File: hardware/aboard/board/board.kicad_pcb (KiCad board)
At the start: 2 copper layers, 68.6 x 53.3 mm, 41 parts, among them J1 Conn_01x04_Male, P1 Power, P2 Analog, P3 Digital, P4 Digital, P5 CONN_01X01, P6 CONN_01X01, P7 CONN_01X01, P8 CONN_01X01, U1 24LC512, U10 ST25DV04K, U2 AT25SF081-SSHD-X, U3 24LC512, U4 AT25SF081-SSHD-X, U5 24LC512, U6 LTC3406ES5, U8 Si5351A, U9 ICE40UP5K-SG48ITR, Y1 Crystal

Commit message: board for OM13088UL: process 4
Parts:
- Y1: value Crystal -> Crystal_GND24; footprint Crystal:Crystal_SMD_5032-2Pin_5.0x3.2mm -> Crystal:Crystal_SMD_5032-4Pin_5.0x3.2mm
- moved U8 29.7 mm to (153.2, 83.7)
- moved Y1 22.0 mm to (147.1, 83.7), turned to 90 degrees
- moved C3 18.3 mm to (152.1, 81.2), turned to 180 degrees
- moved C4 17.8 mm to (156.3, 81.2)
- moved U5 9.19 mm to (147.1, 90.8)
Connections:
- Y1 pad 1: Net-(U8-Pad2) -> Net-(U8-Pad3)
- Y1 pad 2: Net-(U8-Pad3) -> GND
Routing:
- net +3V3: track 0.00 -> 109.4 mm
- net SCL: track 32.0 -> 13.9 mm
- net SDA: track 31.4 -> 18.1 mm
- net Net-(U8-Pad2): track 0.00 -> 7.12 mm
- net Net-(U8-Pad3): track 0.00 -> 3.67 mm
- net GND: track 0.00 -> 1.08 mm, vias 0 -> 14

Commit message: board for OM13088UL: process 5
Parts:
- moved C5 48.3 mm to (114.6, 83.4), turned to 90 degrees
- moved C7 45.2 mm to (113.9, 89.5), turned to 90 degrees
- moved C15 42.4 mm to (119.4, 122.7), turned to 90 degrees
- moved C14 38.6 mm to (115.8, 111.4), turned to 90 degrees
- moved C16 37.1 mm to (122.7, 116.7)
- moved C12 36.7 mm to (118.3, 104.1), turned to 270 degrees
- moved C2 34.4 mm to (133.3, 118.2), turned to 90 degrees
- moved C6 31.7 mm to (129.0, 87.9)
- moved C13 31.2 mm to (128.8, 113.2), turned to 90 degrees
- moved R2 27.8 mm to (138.0, 115.8), turned to 180 degrees
- moved U6 27.8 mm to (138.8, 118.7)
- moved L1 26.9 mm to (134.6, 122.6)
- moved R3 22.7 mm to (167.3, 102.4)
- moved U2 21.2 mm to (164.8, 108.4)
- moved U4 21.2 mm to (161.9, 113.9)
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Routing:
- net +3V3: track 109.4 -> 203.9 mm, vias 0 -> 7
- net CSFPGA: track 0.00 -> 78.2 mm, vias 0 -> 5
- net CDONE: track 0.00 -> 66.8 mm, vias 0 -> 3
- net CRESET: track 0.00 -> 62.5 mm, vias 0 -> 3
- net 1V8: track 0.00 -> 62.4 mm, vias 0 -> 2
- net MISO: track 0.00 -> 53.8 mm, vias 0 -> 3
- net SCK: track 0.00 -> 53.3 mm, vias 0 -> 3
- net MOSI: track 0.00 -> 52.0 mm, vias 0 -> 3
- net Net-(R1-Pad2): track 0.00 -> 5.71 mm
- net Net-(L1-Pad2): track 0.00 -> 3.51 mm
- net GND: track 1.08 -> 3.83 mm, vias 14 -> 94

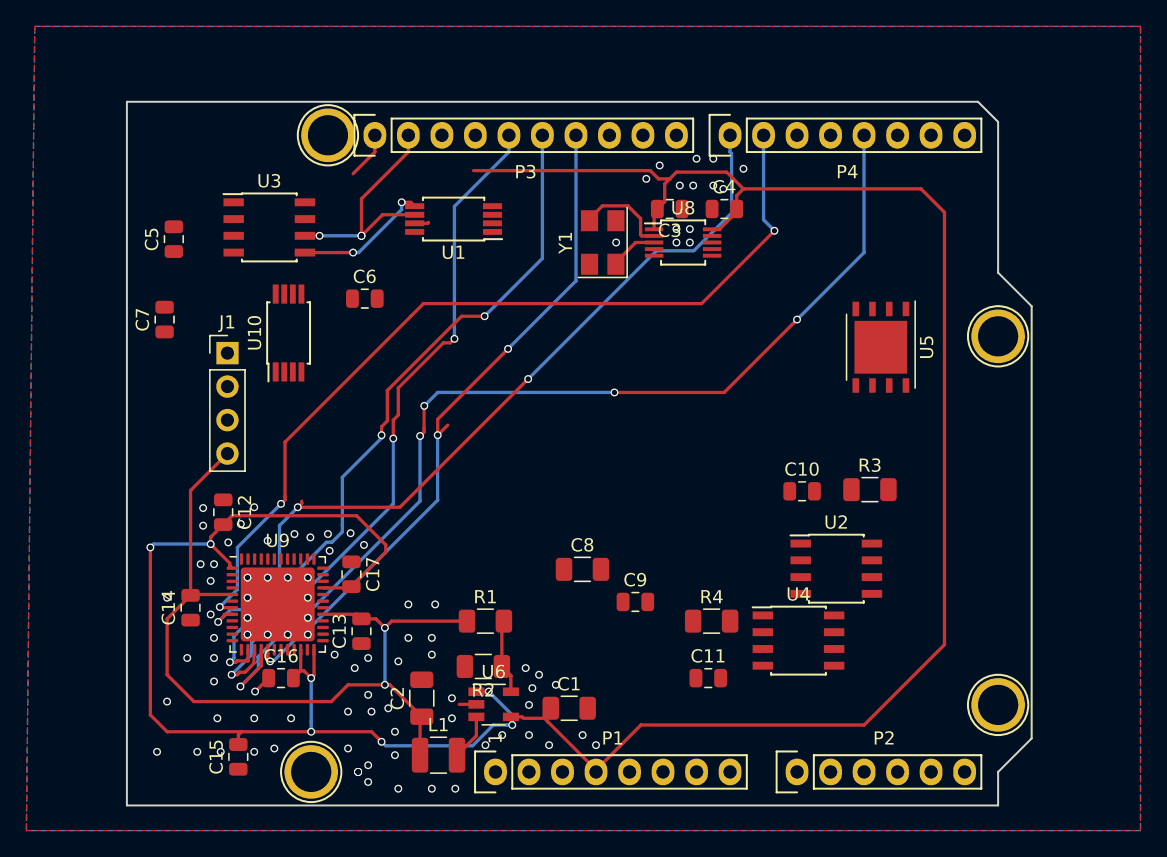
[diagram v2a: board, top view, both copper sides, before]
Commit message: board for OM13088UL: process 6
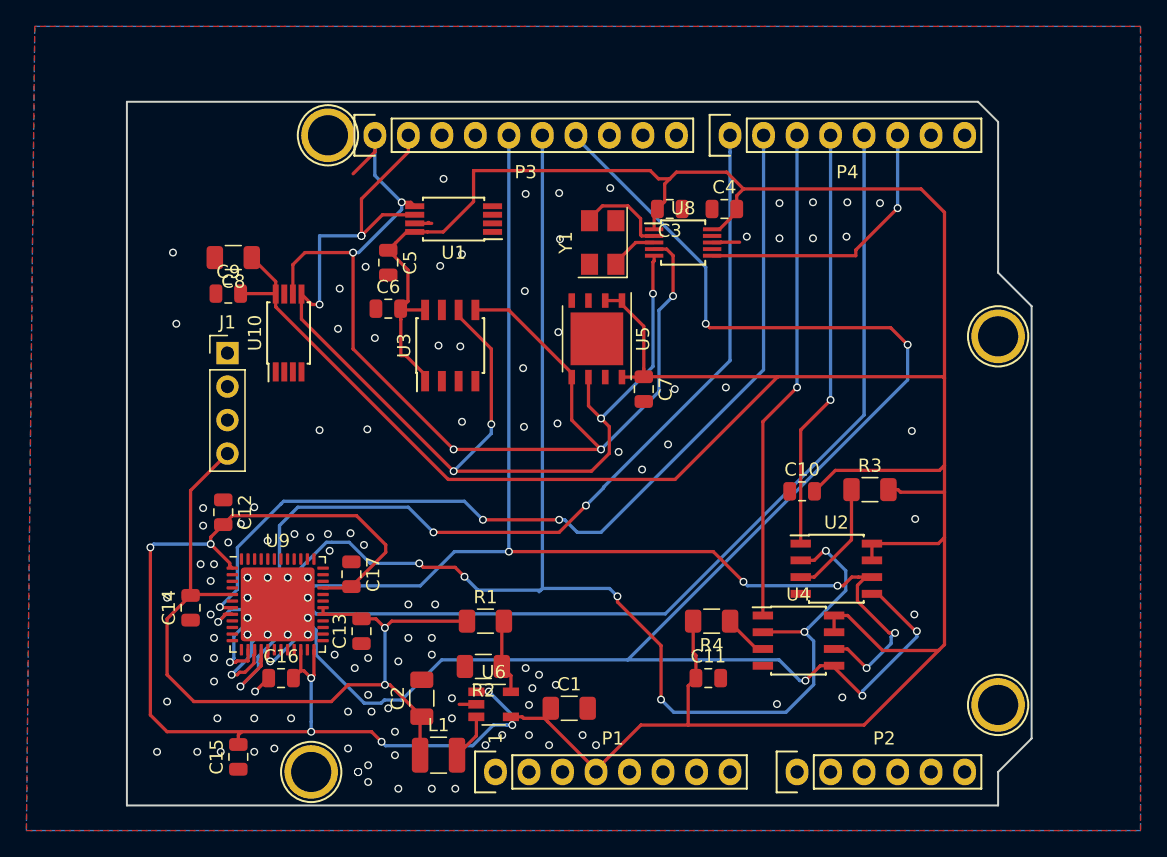
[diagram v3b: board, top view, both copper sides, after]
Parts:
- moved C9 38.7 mm to (118.7, 87.6)
- moved C7 36.7 mm to (150.2, 94.8), turned to 270 degrees
- moved C8 35.5 mm to (119.1, 84.8), turned to 180 degrees
- moved U5 21.5 mm to (146.6, 91.0)
- moved U3 16.4 mm to (135.5, 91.5), turned to 90 degrees
- moved C5 16.4 mm to (130.8, 85.2), turned to 270 degrees
- moved C6 1.93 mm to (130.8, 88.7)
- turned R4 to 180 degrees
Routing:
- net +3V3: track 203.9 -> 354.5 mm
- net MOSI: track 52.0 -> 132.3 mm, vias 3 -> 6
- net SCL: track 13.9 -> 87.2 mm, vias 2 -> 5
- net SDA: track 18.1 -> 89.3 mm, vias 3 -> 7
- net MISO: track 53.8 -> 113.0 mm, vias 3 -> 7
- net SCK: track 53.3 -> 102.2 mm, vias 3 -> 6
- net CSFLASH1: track 0.00 -> 37.5 mm, vias 0 -> 1
- net CSFLASH0: track 0.00 -> 31.9 mm, vias 0 -> 1
- net COUNTER: track 0.00 -> 22.6 mm, vias 0 -> 1
- net Net-(R3-Pad1): track 0.00 -> 8.82 mm
- net CRESET: track 62.5 -> 70.0 mm
- net CDONE: track 66.8 -> 71.2 mm
- net CSFPGA: track 78.2 -> 81.9 mm, vias 5 -> 1
- net Net-(R4-Pad1): track 0.00 -> 3.42 mm
- net GND: track 3.83 -> 6.23 mm, vias 94 -> 121
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
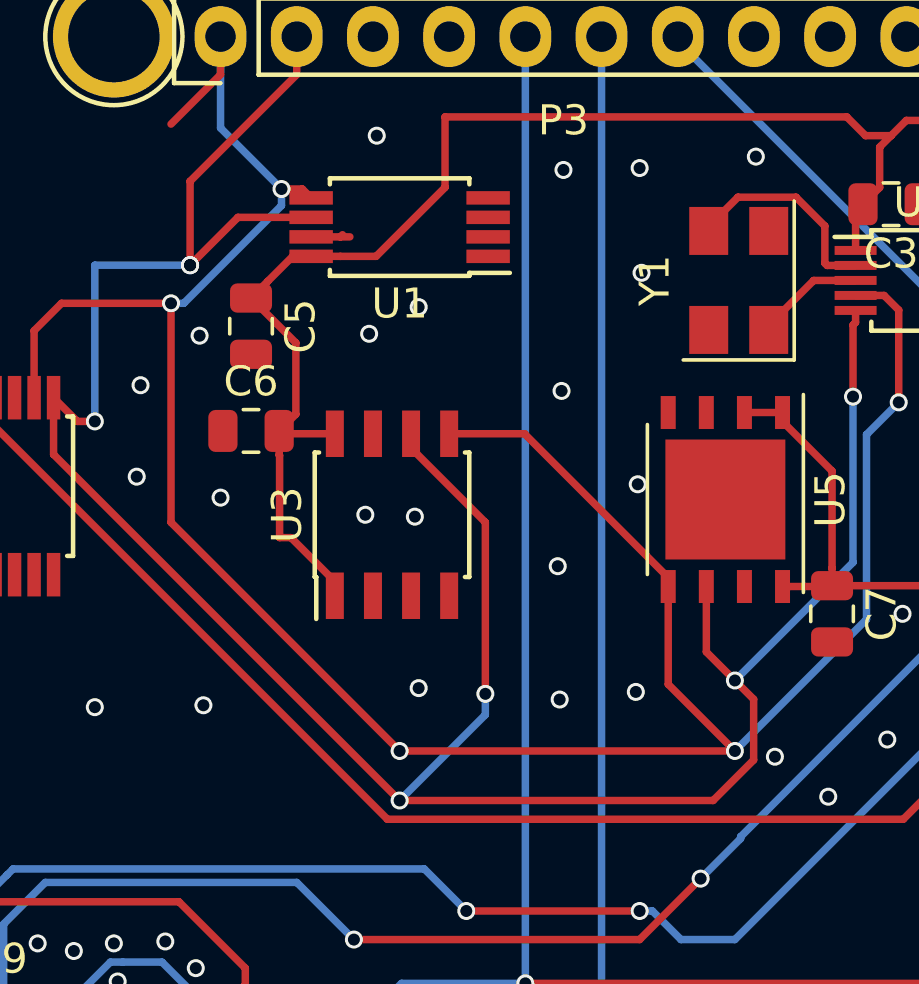
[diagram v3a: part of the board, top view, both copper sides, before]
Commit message: board for OM13088UL: fixed SCL/SDA issue
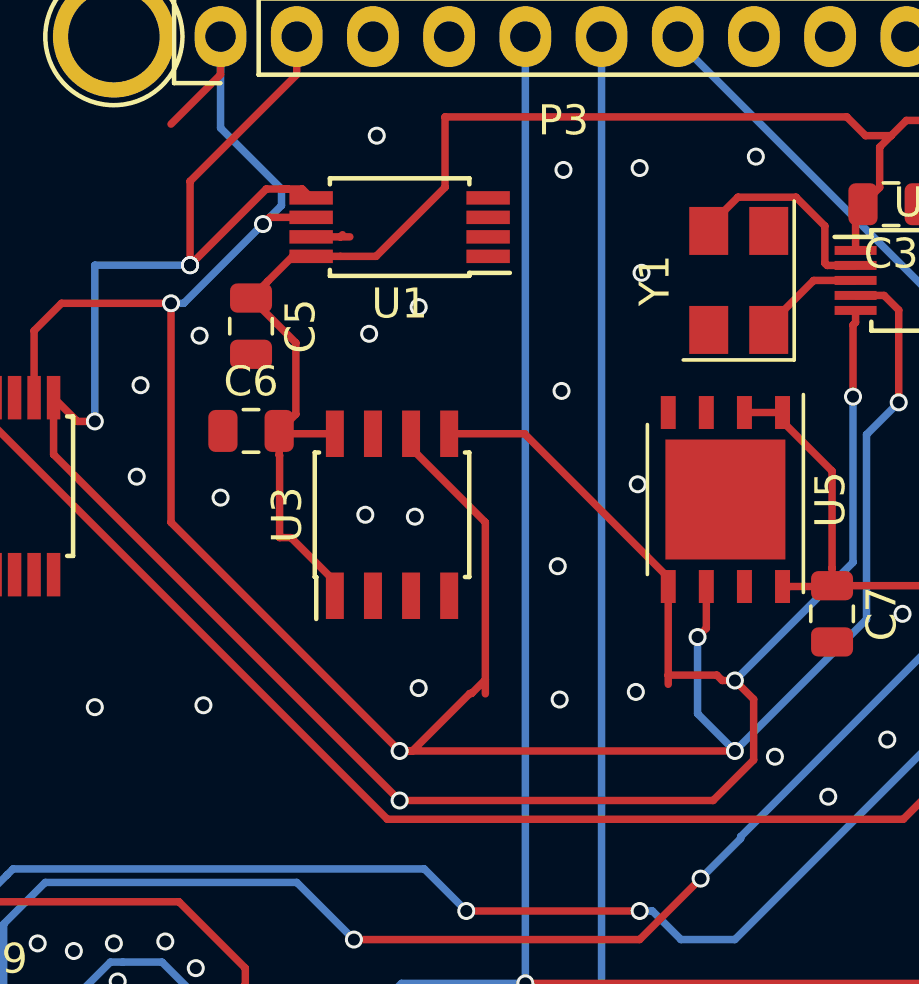
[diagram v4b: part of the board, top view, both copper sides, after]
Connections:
- U1 pad 5: SCL -> SDA
- U1 pad 6: SDA -> SCL
- U3 pad 5: SCL -> SDA
- U3 pad 6: SDA -> SCL
- U5 pad 5: SCL -> SDA
- U5 pad 6: SDA -> SCL
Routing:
- net SCL: track 87.2 -> 91.5 mm, vias 5 -> 6
- net SDA: track 89.3 -> 87.2 mm, vias 7 -> 6
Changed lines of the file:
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@@
     (thickness 1.6)
     (drawings 27)
-    (tracks 588)
+    (tracks 600)
     (zones 0)
     (modules 41)
@@
       (net 4 GND))
     (pad 5 smd rect (at 2.95 0.975 180) (size 1.45 0.45) (layers F.Cu F.Paste F.Mask)
+      (net 29 SDA))
+    (pad 6 smd rect (at 2.95 0.325 180) (size 1.45 0.45) (layers F.Cu F.Paste F.Mask)
       (net 28 SCL))
-    (pad 6 smd rect (at 2.95 0.325 180) (size 1.45 0.45) (layers F.Cu F.Paste F.Mask)
-      (net 29 SDA))
     (pad 7 smd rect (at 2.95 -0.325 180) (size 1.45 0.45) (layers F.Cu F.Paste F.Mask)
       (net 4 GND))
@@
       (net 4 GND))
     (pad 5 smd rect (at 2.7 1.905 90) (size 1.55 0.6) (layers F.Cu F.Paste F.Mask)
+      (net 29 SDA))
+    (pad 6 smd rect (at 2.7 0.635 90) (size 1.55 0.6) (layers F.Cu F.Paste F.Mask)
       (net 28 SCL))
-    (pad 6 smd rect (at 2.7 0.635 90) (size 1.55 0.6) (layers F.Cu F.Paste F.Mask)
-      (net 29 SDA))
     (pad 7 smd rect (at 2.7 -0.635 90) (size 1.55 0.6) (layers F.Cu F.Paste F.Mask)
       (net 4 GND))
@@
       (net 4 GND))
     (pad 5 smd rect (at 2.9 1.905 180) (size 0.5 1.1) (layers F.Cu F.Paste F.Mask)
+      (net 29 SDA))
+    (pad 6 smd rect (at 2.9 0.635 180) (size 0.5 1.1) (layers F.Cu F.Paste F.Mask)
       (net 28 SCL))
-    (pad 6 smd rect (at 2.9 0.635 180) (size 0.5 1.1) (layers F.Cu F.Paste F.Mask)
-      (net 29 SDA))
     (pad 7 smd rect (at 2.9 -0.635 180) (size 0.5 1.1) (layers F.Cu F.Paste F.Mask)
       (net 4 GND))
@@
   (via (at 128.143 84.455) (size 0.6) (drill 0.4) (layers F.Cu B.Cu) (net 28))
   (segment (start 131.826 81.196264) (end 131.826 80.645) (width 0.25) (layer B.Cu) (net 28))
-  (via (at 131.826 80.645) (size 0.6) (drill 0.4) (layers F.Cu B.Cu) (net 28))
   (segment (start 128.143 84.455) (end 128.567264 84.455) (width 0.25) (layer B.Cu) (net 28))
-  (segment (start 128.567264 84.455) (end 131.826 81.196264) (width 0.25) (layer B.Cu) (net 28))
-  (segment (start 132.518 80.645) (end 132.813 80.94) (width 0.25) (layer F.Cu) (net 28))
-  (segment (start 131.826 80.645) (end 132.518 80.645) (width 0.25) (layer F.Cu) (net 28))
+  (segment (start 128.567264 84.455) (end 131.208864 81.8134) (width 0.25) (layer B.Cu) (net 28))
+  (segment (start 132.518 80.645) (end 132.813 80.94) (width 0.25) (layer F.Cu) (net 29))
   (segment (start 151.912 84.193) (end 152.4 84.681) (width 0.25) (layer F.Cu) (net 28))
   (segment (start 150.962 84.193) (end 151.912 84.193) (width 0.25) (layer F.Cu) (net 28))
@@
   (via (at 146.939 99.3775) (size 0.6) (drill 0.4) (layers F.Cu B.Cu) (net 28))
   (segment (start 151.32601 94.99049) (end 146.939 99.3775) (width 0.25) (layer B.Cu) (net 28))
-  (segment (start 144.7165 97.155) (end 144.7165 93.8955) (width 0.25) (layer F.Cu) (net 28))
-  (segment (start 146.939 99.3775) (end 144.7165 97.155) (width 0.25) (layer F.Cu) (net 28))
   (segment (start 146.939 99.3775) (end 135.763 99.3775) (width 0.25) (layer F.Cu) (net 28))
   (via (at 135.763 99.3775) (size 0.6) (drill 0.4) (layers F.Cu B.Cu) (net 28))
-  (segment (start 144.7165 93.5955) (end 144.7165 93.8955) (width 0.25) (layer F.Cu) (net 28))
-  (segment (start 139.9245 88.8035) (end 144.7165 93.5955) (width 0.25) (layer F.Cu) (net 28))
-  (segment (start 137.414 88.8035) (end 139.9245 88.8035) (width 0.25) (layer F.Cu) (net 28))
+  (segment (start 144.7165 93.5955) (end 144.7165 93.8955) (width 0.25) (layer F.Cu) (net 29))
+  (segment (start 139.9245 88.8035) (end 144.7165 93.5955) (width 0.25) (layer F.Cu) (net 29))
+  (segment (start 137.414 88.8035) (end 139.9245 88.8035) (width 0.25) (layer F.Cu) (net 29))
   (segment (start 128.143 91.7575) (end 128.143 84.455) (width 0.25) (layer F.Cu) (net 28))
   (segment (start 135.763 99.3775) (end 128.143 91.7575) (width 0.25) (layer F.Cu) (net 28))
@@
   (via (at 128.778 83.185) (size 0.6) (drill 0.4) (layers F.Cu B.Cu) (net 29))
   (segment (start 128.778 83.185) (end 125.603 83.185) (width 0.25) (layer B.Cu) (net 29))
-  (segment (start 130.373 81.59) (end 132.813 81.59) (width 0.25) (layer F.Cu) (net 29))
-  (segment (start 128.778 83.185) (end 130.373 81.59) (width 0.25) (layer F.Cu) (net 29))
   (segment (start 150.962 85.093) (end 150.876 85.179) (width 0.25) (layer F.Cu) (net 29))
   (segment (start 150.962 84.693) (end 150.962 85.093) (width 0.25) (layer F.Cu) (net 29))
@@
   (via (at 146.939 97.028) (size 0.6) (drill 0.4) (layers F.Cu B.Cu) (net 29))
   (segment (start 150.876 93.091) (end 146.939 97.028) (width 0.25) (layer B.Cu) (net 29))
-  (segment (start 145.9865 96.0755) (end 145.9865 93.8955) (width 0.25) (layer F.Cu) (net 29))
-  (segment (start 146.939 97.028) (end 145.9865 96.0755) (width 0.25) (layer F.Cu) (net 29))
   (segment (start 147.564001 99.677501) (end 146.213002 101.0285) (width 0.25) (layer F.Cu) (net 29))
   (segment (start 146.213002 101.0285) (end 135.763 101.0285) (width 0.25) (layer F.Cu) (net 29))
@@
   (via (at 135.763 101.0285) (size 0.6) (drill 0.4) (layers F.Cu B.Cu) (net 29))
   (segment (start 147.564001 97.653001) (end 147.564001 99.677501) (width 0.25) (layer F.Cu) (net 29))
-  (segment (start 136.144 89.2785) (end 138.6205 91.755) (width 0.25) (layer F.Cu) (net 29))
-  (segment (start 136.144 88.8035) (end 136.144 89.2785) (width 0.25) (layer F.Cu) (net 29))
-  (via (at 138.6205 97.4725) (size 0.6) (drill 0.4) (layers F.Cu B.Cu) (net 29))
-  (segment (start 138.6205 91.755) (end 138.6205 97.4725) (width 0.25) (layer F.Cu) (net 29))
-  (segment (start 138.6205 98.171) (end 135.763 101.0285) (width 0.25) (layer B.Cu) (net 29))
-  (segment (start 138.6205 97.4725) (end 138.6205 98.171) (width 0.25) (layer B.Cu) (net 29))
+  (segment (start 136.144 89.2785) (end 138.6205 91.755) (width 0.25) (layer F.Cu) (net 28))
+  (segment (start 136.144 88.8035) (end 136.144 89.2785) (width 0.25) (layer F.Cu) (net 28))
+  (segment (start 136.187264 99.3775) (end 138.104964 97.4598) (width 0.25) (layer F.Cu) (net 28))
+  (segment (start 135.763 99.3775) (end 136.187264 99.3775) (width 0.25) (layer F.Cu) (net 28))
+  (segment (start 138.1633 97.4598) (end 138.6205 97.0026) (width 0.25) (layer F.Cu) (net 28))
+  (segment (start 138.104964 97.4598) (end 138.1633 97.4598) (width 0.25) (layer F.Cu) (net 28))
+  (segment (start 138.6205 91.755) (end 138.6205 97.0026) (width 0.25) (layer F.Cu) (net 28))
+  (segment (start 138.6205 97.0026) (end 138.6205 97.4725) (width 0.25) (layer F.Cu) (net 28))
+  (via (at 145.6944 95.5802) (size 0.6) (drill 0.4) (layers F.Cu B.Cu) (net 28))
+  (segment (start 145.9865 93.8955) (end 145.9865 95.2881) (width 0.25) (layer F.Cu) (net 28))
+  (segment (start 145.9865 95.2881) (end 145.6944 95.5802) (width 0.25) (layer F.Cu) (net 28))
+  (segment (start 145.6944 98.1329) (end 146.939 99.3775) (width 0.25) (layer B.Cu) (net 28))
+  (segment (start 145.6944 95.5802) (end 145.6944 98.1329) (width 0.25) (layer B.Cu) (net 28))
+  (segment (start 131.208864 81.8134) (end 131.826 81.196264) (width 0.25) (layer B.Cu) (net 28))
+  (via (at 131.208864 81.8134) (size 0.6) (drill 0.4) (layers F.Cu B.Cu) (net 28))
+  (segment (start 131.432264 81.59) (end 132.813 81.59) (width 0.25) (layer F.Cu) (net 28))
+  (segment (start 131.208864 81.8134) (end 131.432264 81.59) (width 0.25) (layer F.Cu) (net 28))
   (segment (start 124.2285 89.494) (end 124.2285 87.601) (width 0.25) (layer F.Cu) (net 29))
   (segment (start 135.763 101.0285) (end 124.2285 89.494) (width 0.25) (layer F.Cu) (net 29))
@@
   (segment (start 125.0195 88.392) (end 124.2285 87.601) (width 0.25) (layer F.Cu) (net 29))
   (segment (start 125.603 88.392) (end 125.0195 88.392) (width 0.25) (layer F.Cu) (net 29))
+  (segment (start 146.514736 97.028) (end 146.336936 96.8502) (width 0.25) (layer F.Cu) (net 29))
+  (segment (start 146.336936 96.8502) (end 144.7165 96.8502) (width 0.25) (layer F.Cu) (net 29))
+  (segment (start 146.939 97.028) (end 146.514736 97.028) (width 0.25) (layer F.Cu) (net 29))
+  (segment (start 144.7165 97.155) (end 144.7165 96.8502) (width 0.25) (layer F.Cu) (net 29))
+  (segment (start 144.7165 96.8502) (end 144.7165 93.8955) (width 0.25) (layer F.Cu) (net 29))
+  (segment (start 128.778 83.185) (end 131.318 80.645) (width 0.25) (layer F.Cu) (net 29))
+  (segment (start 131.318 80.645) (end 132.0292 80.645) (width 0.25) (layer F.Cu) (net 29))
+  (segment (start 131.826 80.645) (end 132.0292 80.645) (width 0.25) (layer F.Cu) (net 29))
+  (segment (start 132.0292 80.645) (end 132.518 80.645) (width 0.25) (layer F.Cu) (net 29))
   (segment (start 119.95291 116.2685) (end 119.95291 116.2685) (width 0.25) (layer F.Cu) (net 30))
   (via (at 118.9355 116.459) (size 0.6) (drill 0.4) (layers F.Cu B.Cu) (net 30))
